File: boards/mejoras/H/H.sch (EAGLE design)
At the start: 20 parts, among them IC1 PIC18F4455_TQFP

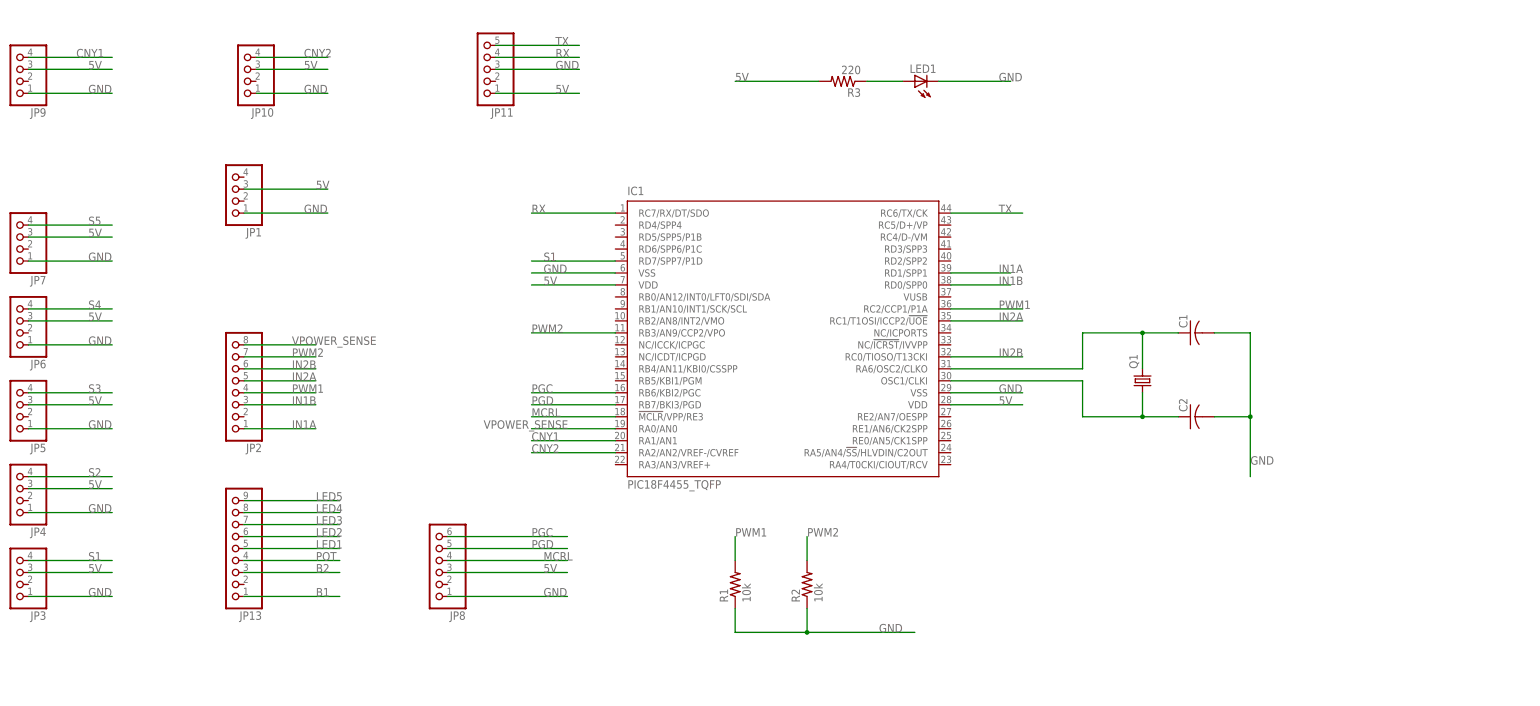
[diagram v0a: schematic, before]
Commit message: added new sumo robot logic start board
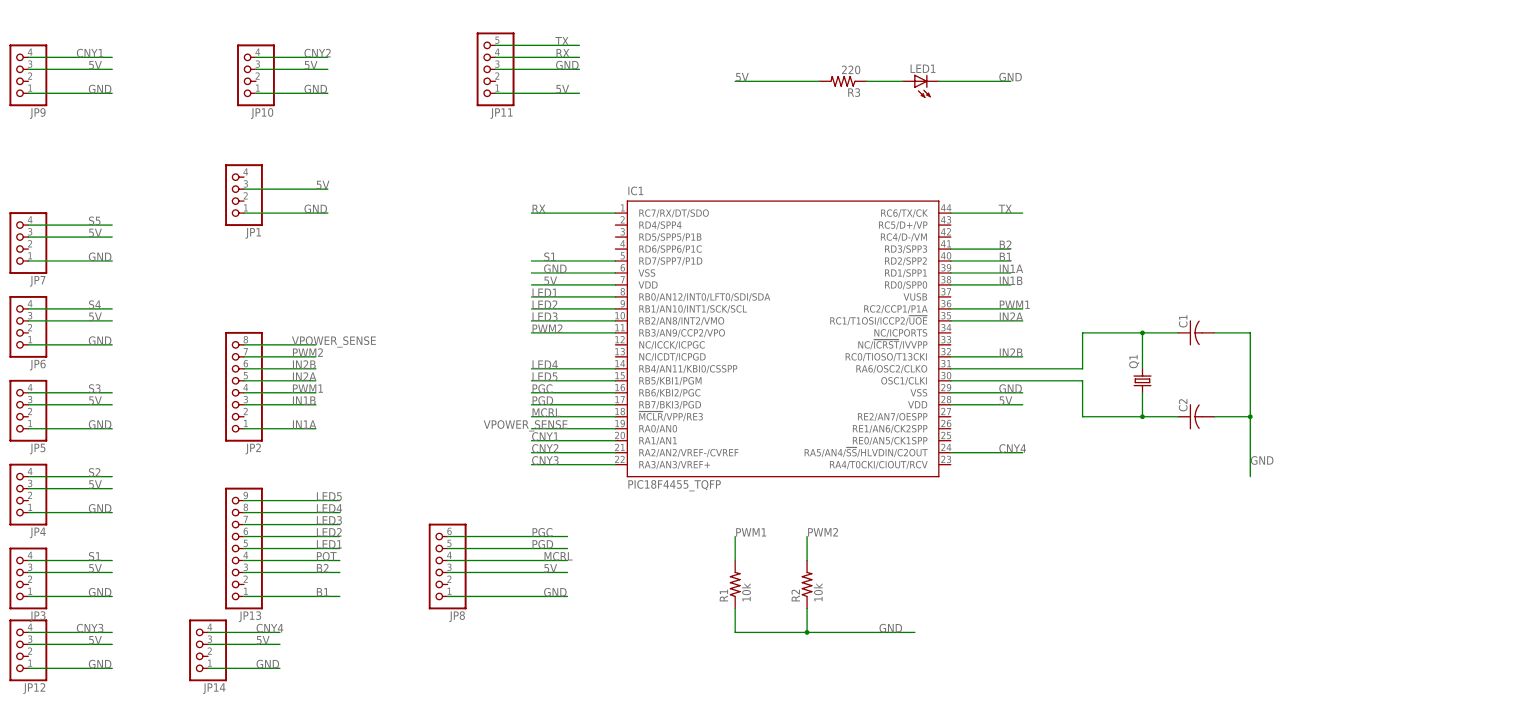
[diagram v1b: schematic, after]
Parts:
- added JP12, JP14: (no value), pinhead-enhanced-3:PINHD-1X4/90
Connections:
- new net CNY3: IC1.RA3/AN3/VREF+, JP12.4
- new net CNY4: IC1.RA5/AN4/!SS!/HLVDIN/C2OUT, JP14.4
- net 5V: now also JP12.3, JP14.3
- net B1: now also IC1.RD2/SPP2
- net B2: now also IC1.RD3/SPP3
- net GND: now also JP12.1, JP14.1
- net LED1: now also IC1.RB0/AN12/INT0/LFT0/SDI/SDA
- net LED2: now also IC1.RB1/AN10/INT1/SCK/SCL
- net LED3: now also IC1.RB2/AN8/INT2/VMO
- net LED4: now also IC1.RB4/AN11/KBI0/CSSPP
- net LED5: now also IC1.RB5/KBI1/PGM
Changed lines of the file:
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@@
 <part name="JP8" library="pinhead-enhanced-2" deviceset="PINHD-1X6" device="/90" package3d_urn="urn:adsk.eagle:package:22475/2"/>
 <part name="JP13" library="pinhead-enhanced-3" deviceset="PINHD-1X9" device="/90" package3d_urn="urn:adsk.eagle:package:22482/2"/>
+<part name="JP12" library="pinhead-enhanced-3" deviceset="PINHD-1X4" device="/90" package3d_urn="urn:adsk.eagle:package:22404/2"/>
+<part name="JP14" library="pinhead-enhanced-3" deviceset="PINHD-1X4" device="/90" package3d_urn="urn:adsk.eagle:package:22404/2"/>
 </parts>
 <sheets>
@@
 <attribute name="VALUE" x="-31.75" y="-10.16" size="1.778" layer="96" rot="R180"/>
 </instance>
+<instance part="JP12" gate="A" x="-83.82" y="-45.72" smashed="yes" rot="R180">
+<attribute name="NAME" x="-77.47" y="-53.975" size="1.778" layer="95" rot="R180"/>
+<attribute name="VALUE" x="-77.47" y="-38.1" size="1.778" layer="96" rot="R180"/>
+</instance>
+<instance part="JP14" gate="A" x="-45.72" y="-45.72" smashed="yes" rot="R180">
+<attribute name="NAME" x="-39.37" y="-53.975" size="1.778" layer="95" rot="R180"/>
+<attribute name="VALUE" x="-39.37" y="-38.1" size="1.778" layer="96" rot="R180"/>
+</instance>
 </instances>
 <busses>
@@
 <label x="124.46" y="73.66" size="1.778" layer="95"/>
 </segment>
+<segment>
+<pinref part="JP12" gate="A" pin="1"/>
+<wire x1="-81.28" y1="-50.8" x2="-63.5" y2="-50.8" width="0.1524" layer="91"/>
+<label x="-68.58" y="-50.8" size="1.778" layer="95"/>
+</segment>
+<segment>
+<pinref part="JP14" gate="A" pin="1"/>
+<wire x1="-43.18" y1="-50.8" x2="-27.94" y2="-50.8" width="0.1524" layer="91"/>
+<label x="-33.02" y="-50.8" size="1.778" layer="95"/>
+</segment>
 </net>
 <net name="5V" class="0">
@@
 <wire x1="86.36" y1="73.66" x2="68.58" y2="73.66" width="0.1524" layer="91"/>
 <label x="68.58" y="73.66" size="1.778" layer="95"/>
+</segment>
+<segment>
+<pinref part="JP12" gate="A" pin="3"/>
+<wire x1="-81.28" y1="-45.72" x2="-63.5" y2="-45.72" width="0.1524" layer="91"/>
+<label x="-68.58" y="-45.72" size="1.778" layer="95"/>
+</segment>
+<segment>
+<pinref part="JP14" gate="A" pin="3"/>
+<wire x1="-43.18" y1="-45.72" x2="-27.94" y2="-45.72" width="0.1524" layer="91"/>
+<label x="-33.02" y="-45.72" size="1.778" layer="95"/>
 </segment>
 </net>
@@
 <pinref part="JP13" gate="A" pin="3"/>
 </segment>
+<segment>
+<pinref part="IC1" gate="G$1" pin="RD3/SPP3"/>
+<wire x1="114.3" y1="38.1" x2="127" y2="38.1" width="0.1524" layer="91"/>
+<label x="124.46" y="38.1" size="1.778" layer="95"/>
+</segment>
 </net>
 <net name="POT" class="0">
@@
 <pinref part="JP13" gate="A" pin="5"/>
 </segment>
+<segment>
+<pinref part="IC1" gate="G$1" pin="RB0/AN12/INT0/LFT0/SDI/SDA"/>
+<wire x1="43.18" y1="27.94" x2="25.4" y2="27.94" width="0.1524" layer="91"/>
+<label x="25.4" y="27.94" size="1.778" layer="95"/>
+</segment>
 </net>
 <net name="LED2" class="0">
@@
 <pinref part="JP13" gate="A" pin="6"/>
 </segment>
+<segment>
+<pinref part="IC1" gate="G$1" pin="RB1/AN10/INT1/SCK/SCL"/>
+<wire x1="43.18" y1="25.4" x2="25.4" y2="25.4" width="0.1524" layer="91"/>
+<label x="25.4" y="25.4" size="1.778" layer="95"/>
+</segment>
 </net>
 <net name="LED3" class="0">
@@
 <pinref part="JP13" gate="A" pin="7"/>
 </segment>
+<segment>
+<pinref part="IC1" gate="G$1" pin="RB2/AN8/INT2/VMO"/>
+<wire x1="43.18" y1="22.86" x2="25.4" y2="22.86" width="0.1524" layer="91"/>
+<label x="25.4" y="22.86" size="1.778" layer="95"/>
+</segment>
 </net>
 <net name="LED4" class="0">
@@
 <pinref part="JP13" gate="A" pin="8"/>
 </segment>
+<segment>
+<pinref part="IC1" gate="G$1" pin="RB4/AN11/KBI0/CSSPP"/>
+<wire x1="43.18" y1="12.7" x2="25.4" y2="12.7" width="0.1524" layer="91"/>
+<label x="25.4" y="12.7" size="1.778" layer="95"/>
+</segment>
 </net>
 <net name="S2" class="0">
@@
 <pinref part="JP13" gate="A" pin="1"/>
 </segment>
+<segment>
+<pinref part="IC1" gate="G$1" pin="RD2/SPP2"/>
+<wire x1="114.3" y1="35.56" x2="127" y2="35.56" width="0.1524" layer="91"/>
+<label x="124.46" y="35.56" size="1.778" layer="95"/>
+</segment>
 </net>
 <net name="N$3" class="0">
@@
 <pinref part="JP13" gate="A" pin="9"/>
 </segment>
-</net>
+<segment>
+<pinref part="IC1" gate="G$1" pin="RB5/KBI1/PGM"/>
+<wire x1="43.18" y1="10.16" x2="25.4" y2="10.16" width="0.1524" layer="91"/>
+<label x="25.4" y="10.16" size="1.778" layer="95"/>
+</segment>
+</net>
+<net name="CNY3" class="0">
+<segment>
+<pinref part="JP12" gate="A" pin="4"/>
+<wire x1="-81.28" y1="-43.18" x2="-63.5" y2="-43.18" width="0.1524" layer="91"/>
+<label x="-71.12" y="-43.18" size="1.778" layer="95"/>
+</segment>
+<segment>
+<pinref part="IC1" gate="G$1" pin="RA3/AN3/VREF+"/>
+<wire x1="43.18" y1="-7.62" x2="25.4" y2="-7.62" width="0.1524" layer="91"/>
+<label x="25.4" y="-7.62" size="1.778" layer="95"/>
+</segment>
+</net>
+<net name="CNY4" class="0">
+<segment>
+<pinref part="JP14" gate="A" pin="4"/>
+<wire x1="-43.18" y1="-43.18" x2="-27.94" y2="-43.18" width="0.1524" layer="91"/>
+<label x="-33.02" y="-43.18" size="1.778" layer="95"/>
+</segment>
+<segment>
+<pinref part="IC1" gate="G$1" pin="RA5/AN4/!SS!/HLVDIN/C2OUT"/>
+<wire x1="114.3" y1="-5.08" x2="129.54" y2="-5.08" width="0.1524" layer="91"/>
+<label x="124.46" y="-5.08" size="1.778" layer="95"/>
+</segment>
+</net>

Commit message: added board h first version
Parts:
- added C3, C4: (no value), adafruit:C-USC0805K
- added R10, R11, R12, R4, R5, R6, R7, R8, R9: 10k, adafruit:R-US_M1206
- added R13, R14, R15, R16: 220, adafruit:R-US_M1206
- renumbered JP10 to CNY2, JP12 to CNY3, JP14 to CNY4, JP3 to S1, JP4 to S2, JP5 to S3, JP6 to S4, JP7 to S5, JP8 to PROG, JP9 to CNY1
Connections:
- new net N$4: CNY1.3, R13.2
- new net N$5: CNY2.3, R14.2
- new net N$6: CNY3.3, R15.2
- new net N$7: CNY4.3, R16.2
- net 5V: now also C3.1, R13.1, R14.1, R15.1, R16.1; no longer CNY1.3, CNY2.3, CNY3.3, CNY4.3
- net CNY1: now also IC1.RA2/AN2/VREF-/CVREF, R4.2; no longer IC1.RA1/AN1
- net CNY2: now also IC1.RA3/AN3/VREF+, R5.2; no longer IC1.RA2/AN2/VREF-/CVREF
- net CNY3: now also IC1.RA5/AN4/!SS!/HLVDIN/C2OUT, R6.2; no longer IC1.RA3/AN3/VREF+
- net CNY4: now also IC1.RE0/AN5/CK1SPP, R7.2; no longer IC1.RA5/AN4/!SS!/HLVDIN/C2OUT
- net GND: now also C3.2, C4.2, R10.1, R11.1, R12.1, R4.1, R5.1, R6.1, R7.1, R8.1, R9.1
- net POT: now also IC1.RA0/AN0
- net PWM1: now also IC1.RB3/AN9/CCP2/VPO; no longer IC1.RC2/CCP1/P1A
- net PWM2: now also IC1.RC2/CCP1/P1A; no longer IC1.RB3/AN9/CCP2/VPO
- net S1: now also R8.2
- net S2: now also IC1.RD6/SPP6/P1C, R9.2
- net S3: now also IC1.RD5/SPP5/P1B, R10.2
- net S4: now also IC1.RD4/SPP4, R11.2
- net S5: now also IC1.RC5/D+/VP, R12.2
- net VPOWER_SENSE: now also C4.1, IC1.RA1/AN1; no longer IC1.RA0/AN0

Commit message: updated boards
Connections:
- net 5V: now also R4.1, R5.1, R6.1, R7.1
- net GND: no longer R4.1, R5.1, R6.1, R7.1
